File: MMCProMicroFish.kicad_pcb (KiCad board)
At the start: 2 copper layers, 18 x 35.2 mm, 25 parts, among them J1 USB2_C_Receptacle, J2 Conn_01x12, J3 Conn_01x12, J4 Conn_01x05, U1 ATmega32U4-AU, X1 Resonator

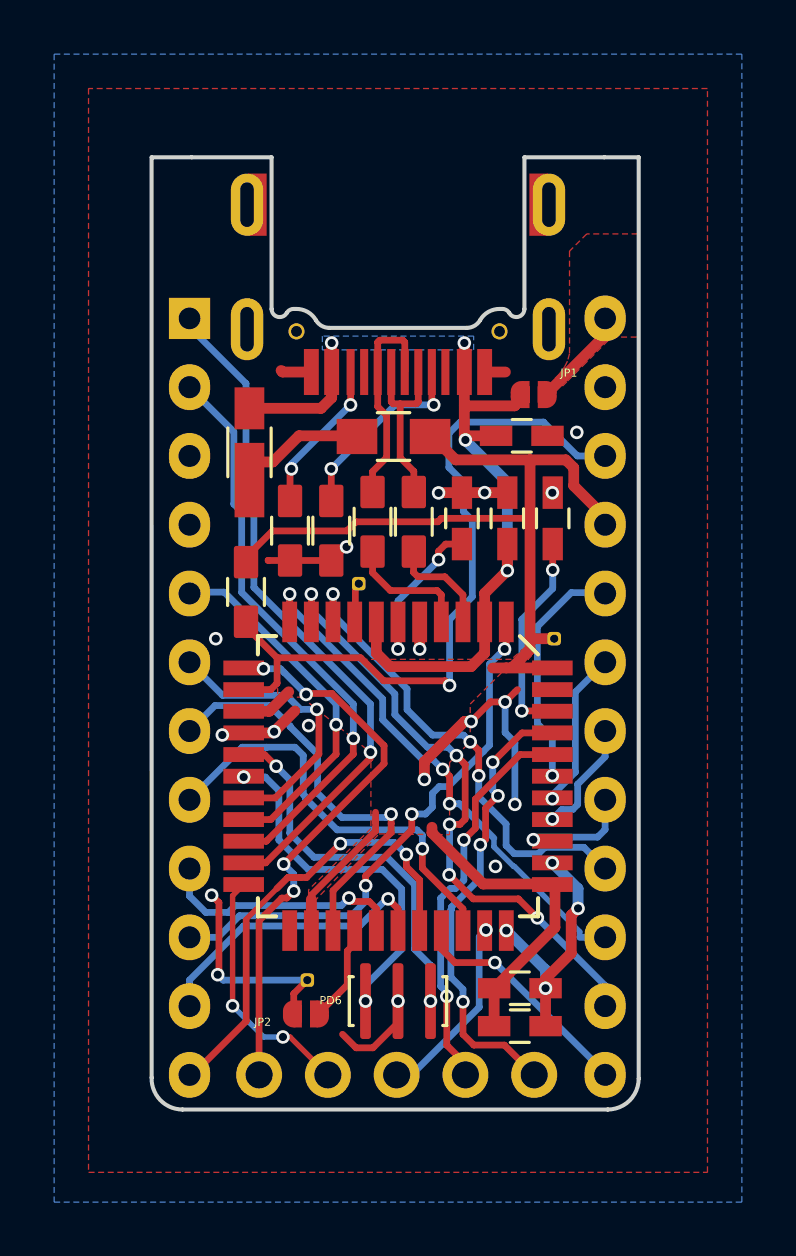
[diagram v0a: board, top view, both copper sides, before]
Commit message: Rerouted
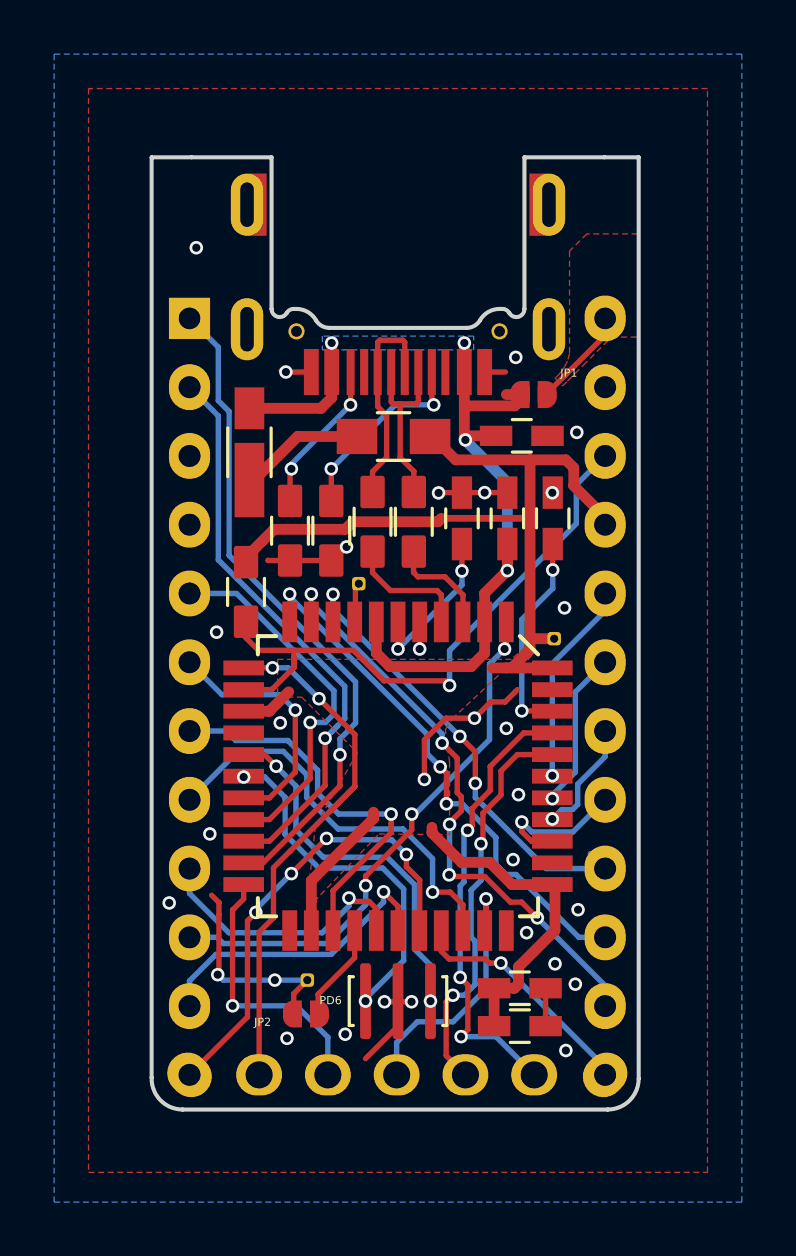
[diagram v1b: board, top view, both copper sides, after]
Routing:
- net GND: track 41.2 -> 27.0 mm, vias 22 -> 30
- net RESET: track 27.4 -> 22.9 mm
- net PC7: track 7.52 -> 10.3 mm
- net PD0: track 10.6 -> 9.23 mm
- net PB1: track 18.6 -> 17.4 mm
- net PD4: track 16.1 -> 14.9 mm
- net PF4: track 8.79 -> 7.56 mm
- net PD5: track 9.36 -> 10.2 mm, vias 2 -> 1
- net PB2: track 23.2 -> 22.4 mm
- net PD7: track 9.55 -> 10.3 mm
- net PF7: track 4.63 -> 5.35 mm
- net VBUS: track 28.4 -> 28.9 mm
- net PD2: track 21.4 -> 21.9 mm
- net PB7: track 21.4 -> 21.0 mm, vias 4 -> 2
- net PF0: track 17.5 -> 17.4 mm, vias 4 -> 3
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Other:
- net class Default: clearance 0.127 -> 0.2; trace_width 0.25 -> 0.2
- rule trace_clearance: 0.127 -> 0.2
- board text added: "DingRev 2020 LONGBOI"
- board text removed: "B3"
- board text removed: "DingRev 2020"
